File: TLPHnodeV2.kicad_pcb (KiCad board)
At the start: 4 copper layers, 28 x 20.5 mm, 30 parts, among them P1 Bat, P2 CONN_01X07, SW1 Reset, U1 NCP703, U2 LD39130S, U3 LPS25HB, U4 Si7006-A20, U5 ESP-12E, U6 ISL29035

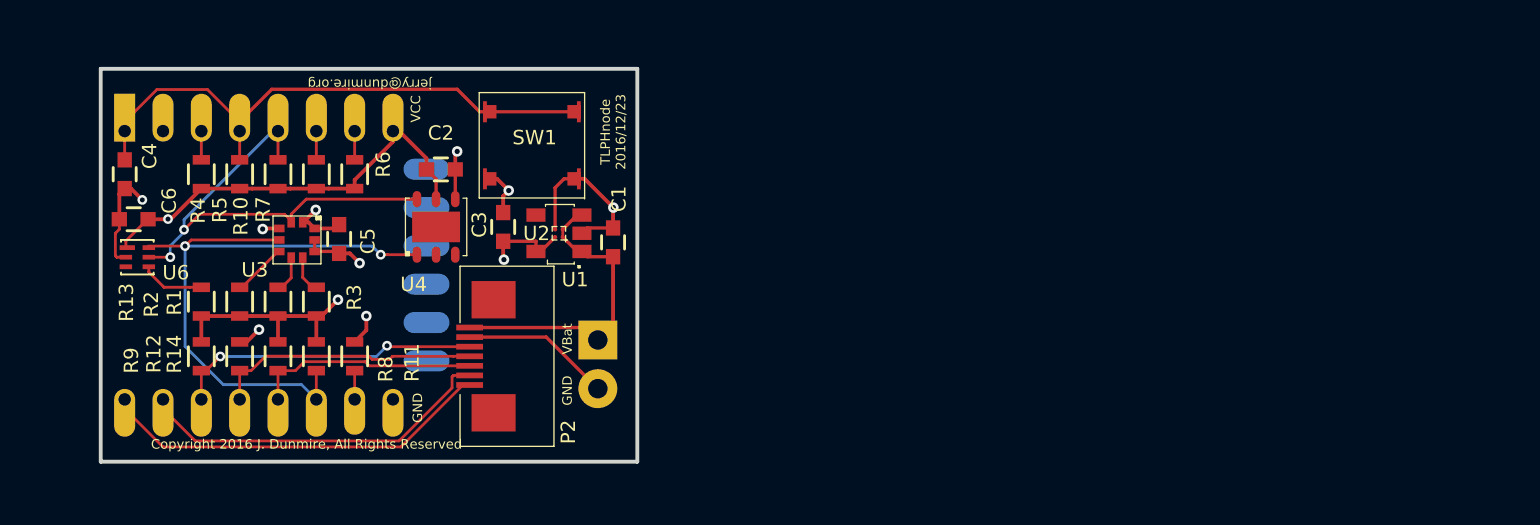
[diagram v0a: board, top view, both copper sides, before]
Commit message: Get ready for new routing
    - remove old parts and all traces
    - import new netlist

On branch master
modified:   TLPHnodeV2.kicad_pcb
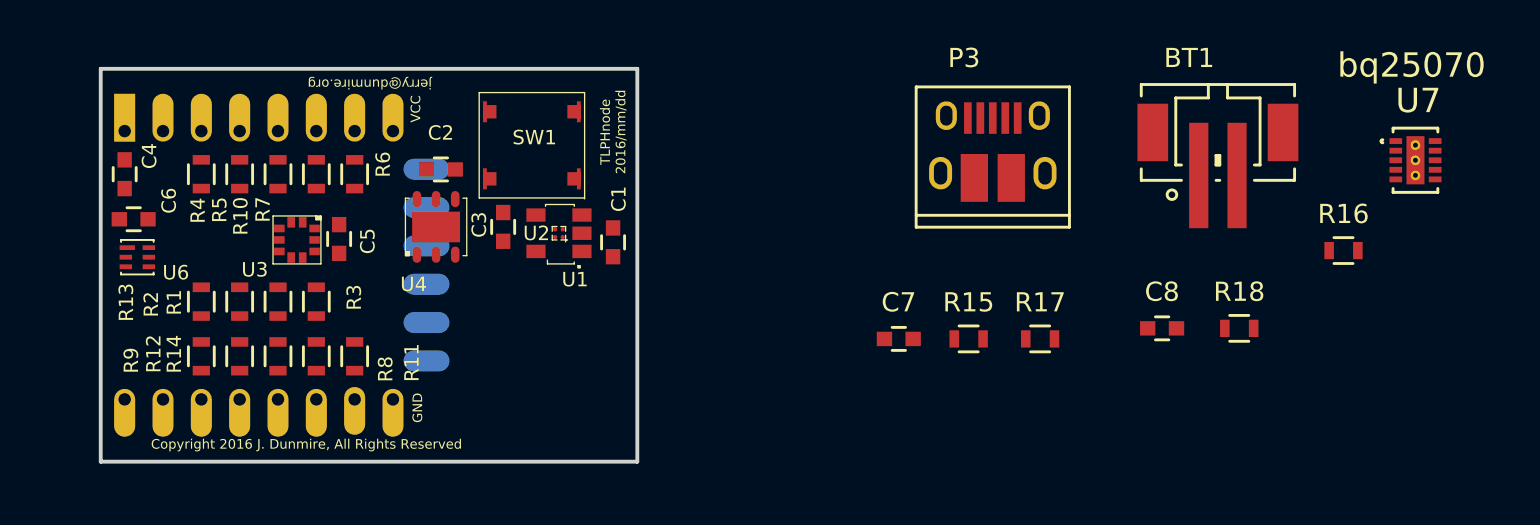
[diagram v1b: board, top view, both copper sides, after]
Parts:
- removed P1: Bat, Pin_Headers:Pin_Header_Straight_1x02
- removed P2: CONN_01X07, rockingdlabs:FPC_conn-7_8x4.9mm_Pitch0.5mm
- removed Ref**: RockingDLogo_9x7, rockingDLogos:RockingDLogo_9x7
- added BT1: LiFeP04, Connectors_JST:JST_PH_B2B-PH-SM4-TB_02x2.00mm_Straight, F.Cu at (188.8, 84.9)
- added C7: 1 uF, Capacitors_SMD:C_0603, F.Cu at (172.1, 94.6)
- added C8: 2 uF, Capacitors_SMD:C_0603, F.Cu at (185.9, 94.0)
- added P3: USB (power only), Connect:USB_Micro-B_10103594-0001LF, F.Cu at (177.1, 84.6)
- added R15: 10k, Resistors_SMD:R_0603, F.Cu at (175.8, 94.6)
- added R16: 1k, Resistors_SMD:R_0603, F.Cu at (195.3, 90.0)
- added R17: 487k, Resistors_SMD:R_0603, F.Cu at (179.5, 94.6)
- added R18: 100k, Resistors_SMD:R_0603, F.Cu at (189.9, 94.0)
- added U7: bq25070, rockingdlabs:bq25070_DQC_10-DQC10_P84X2P4, F.Cu at (199.1, 85.3)
- R12: value 10k -> 4.7k
- R14: value 4.7k -> 10k
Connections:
- net /CHRG renamed /node/CHRG
- net /I2C_SCL renamed /node/I2C_SCL
- net /I2C_SDA renamed /node/I2C_SDA
- net /VBat renamed +BATT
- R12 pad 1: /CTRL -> VCC
- R12 pad 2: GND -> Net-(R12-Pad2)
- R13 pad 2: Net-(R13-Pad2) -> /node/PGM
- R14 pad 1: VCC -> /node/CTRL
- R14 pad 2: /PGM -> GND
- U1 pad 4: Net-(U1-Pad4) -> (no net)
- U5 pad 12: /PGM -> /node/PGM
- U5 pad 13: /CTRL -> /node/CTRL
- U5 pad 15: /RXD -> /node/RXD
- U5 pad 16: /TXD -> /node/TXD
- U5 pad 17: Net-(U5-Pad17) -> (no net)
- U5 pad 18: Net-(U5-Pad18) -> (no net)
- U5 pad 19: Net-(U5-Pad19) -> (no net)
- U5 pad 2: Net-(U5-Pad2) -> (no net)
- U5 pad 20: Net-(U5-Pad20) -> (no net)
- U5 pad 21: Net-(U5-Pad21) -> (no net)
- U5 pad 22: Net-(U5-Pad22) -> (no net)
- U6 pad 3: Net-(U6-Pad3) -> (no net)
- U6 pad 4: Net-(R13-Pad2) -> Net-(R12-Pad2)
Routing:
- net VCC: track 41.0 -> 0.00 mm, vias 4 -> 0
- net GND: track 34.1 -> 0.00 mm, vias 8 -> 0
- net /node/I2C_SDA: track 34.0 -> 0.00 mm, vias 2 -> 0
- net Net-(C4-Pad1): track 30.5 -> 0.00 mm
- net /node/I2C_SCL: track 25.1 -> 0.00 mm, vias 2 -> 0
- net /TXD: track 20.6 -> 0.00 mm
- net /RXD: track 18.9 -> 0.00 mm
- net +BATT: track 16.4 -> 0.00 mm
- net /node/CHRG: track 16.1 -> 0.00 mm, vias 2 -> 0
- net /CTRL: track 13.9 -> 0.00 mm
- net /PGM: track 11.8 -> 0.00 mm
- net Net-(R13-Pad2): track 3.34 -> 0.00 mm
- net Net-(R2-Pad2): track 2.84 -> 0.00 mm
- net Net-(R3-Pad2): track 1.96 -> 0.00 mm
- net Net-(R1-Pad2): track 1.95 -> 0.00 mm
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- removed copper zone on In1.Cu.GND, net GND
- removed copper zone on In2.Cu.VCC, net VCC
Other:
- board text added: "TLPHnode 2016/mm/dd"
- board text removed: "TLPHnode 2016/12/23"
- board text removed: "VBat"

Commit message: CP- initial placement
On branch master
modified:   TLPHnodeV2.kicad_pcb
modified:   TLPHnodeV2.pro
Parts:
- removed C1: 1 uF, Capacitors_SMD:C_0603
- removed R14: 10k, Resistors_SMD:R_0603
- BT1, P3: moved to B.Cu
- moved U7 49.8 mm to (150.5, 96.0), turned to 180 degrees
- moved R16 41.9 mm to (153.8, 95.2)
- moved R15 37.1 mm to (138.8, 95.5), turned to 90 degrees
- moved R18 36.0 mm to (154.0, 91.8)
- moved C8 35.4 mm to (150.5, 93.5)
- moved BT1 35.1 mm to (153.8, 86.2), turned to 90 degrees
- moved P3 24.8 mm to (155.0, 96.0), turned to 270 degrees
- moved R17 22.8 mm to (156.9, 91.8), turned to 180 degrees
- moved C7 18.6 mm to (153.8, 97.0)
- moved R12 5.40 mm to (132.5, 94.2)
- moved R13 5.33 mm to (140.2, 95.5), turned to 270 degrees
- moved U1 4.02 mm to (150.8, 90.9), turned to 180 degrees
- moved U2 3.97 mm to (150.8, 90.8), turned to 90 degrees
- moved U4 3.75 mm to (145.8, 91.8)
- moved C2 3.55 mm to (146.0, 88.5)
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
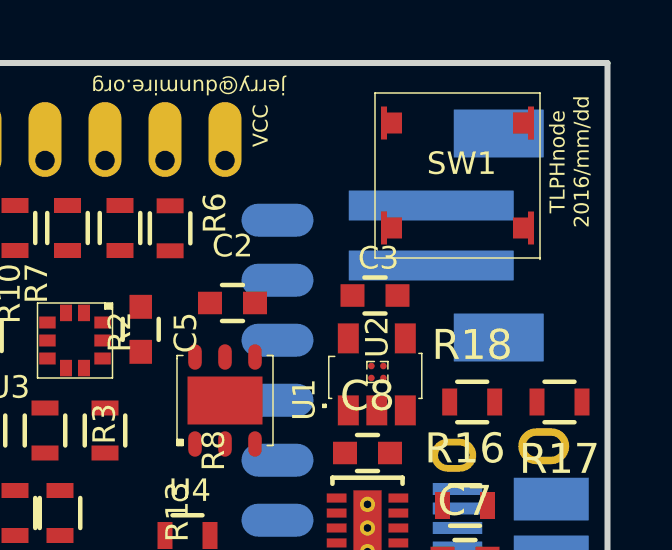
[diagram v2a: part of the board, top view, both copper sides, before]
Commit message: CP - refined placement
    - Rotated battery connector
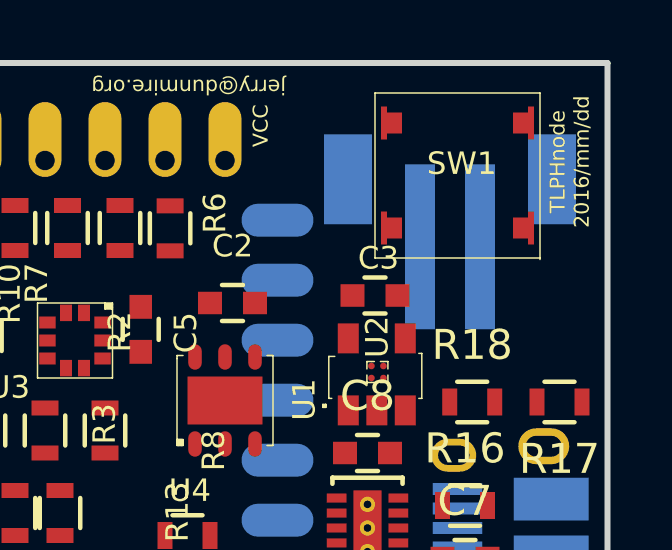
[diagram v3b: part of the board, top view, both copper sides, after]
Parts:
- moved BT1 0.90 mm to (153.2, 85.5), turned to 180 degrees
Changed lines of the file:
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@@
   )
   (module Connectors_JST:JST_PH_B2B-PH-SM4-TB_02x2.00mm_Straight (layer B.Cu)
-    (at 153.75 86.25 90)
+    (at 153.25 85.5 180)
     (descr http://www.jst-mfg.com/product/pdf/eng/ePH.pdf)
     (tags "connector jst ph")
     (attr smd)
-    (fp_text reference BT1 (at -1.5 5 90) (layer B.SilkS)
+    (fp_text reference BT1 (at -1.5 5 180) (layer B.SilkS)
       (effects (font (size 1 1) (thickness 0.15)) (justify mirror))
     )
-    (fp_text value LiFeP04 (at 0 -5.25 90) (layer B.Fab)
+    (fp_text value LiFeP04 (at 0 -5.25 180) (layer B.Fab)
       (effects (font (size 1 1) (thickness 0.15)) (justify mirror))
     )
@@
     (fp_line (start -4 3.025) (end -4 3.625) (layer B.SilkS) (width 0.15))
     (fp_circle (center -2.4 -2.125) (end -2.15 -2.125) (layer B.SilkS) (width 0.15))
-    (pad "" smd rect (at 3.4 1.125 90) (size 1.6 3) (layers B.Cu B.Paste B.Mask))
-    (pad "" smd rect (at -3.4 1.125 90) (size 1.6 3) (layers B.Cu B.Paste B.Mask))
-    (pad 2 smd rect (at 1 -1.125 90) (size 1 5.5) (layers B.Cu B.Paste B.Mask)
+    (pad "" smd rect (at 3.4 1.125 180) (size 1.6 3) (layers B.Cu B.Paste B.Mask))
+    (pad "" smd rect (at -3.4 1.125 180) (size 1.6 3) (layers B.Cu B.Paste B.Mask))
+    (pad 2 smd rect (at 1 -1.125 180) (size 1 5.5) (layers B.Cu B.Paste B.Mask)
       (net 1 GND))
-    (pad 1 smd rect (at -1 -1.125 90) (size 1 5.5) (layers B.Cu B.Paste B.Mask)
+    (pad 1 smd rect (at -1 -1.125 180) (size 1 5.5) (layers B.Cu B.Paste B.Mask)
       (net 11 +BATT))
+    (model ${ROCKINGDLIB}/rockingdlabs.3dshapes/B2B-PH-SM4-TB.STEP
+      (at (xyz -0.1574803149606299 0.09842519685039371 0))
+      (scale (xyz 1 1 1))
+      (rotate (xyz -90 0 0))
+    )
   )
   (module Capacitors_SMD:C_0603 (layer F.Cu)
@@
     (pad 1 smd rect (at -1.3 1.5 180) (size 1.65 0.4) (layers B.Cu B.Paste B.Mask)
       (net 12 /power/VDD))
+    (model ${ROCKINGDLIB}/rockingdlabs.3dshapes/10103594.stp
+      (at (xyz 0 0 0.08858267716535434))
+      (scale (xyz 1 1 1))
+      (rotate (xyz 90 0 180))
+    )
   )
   (module Resistors_SMD:R_0603 (layer F.Cu)

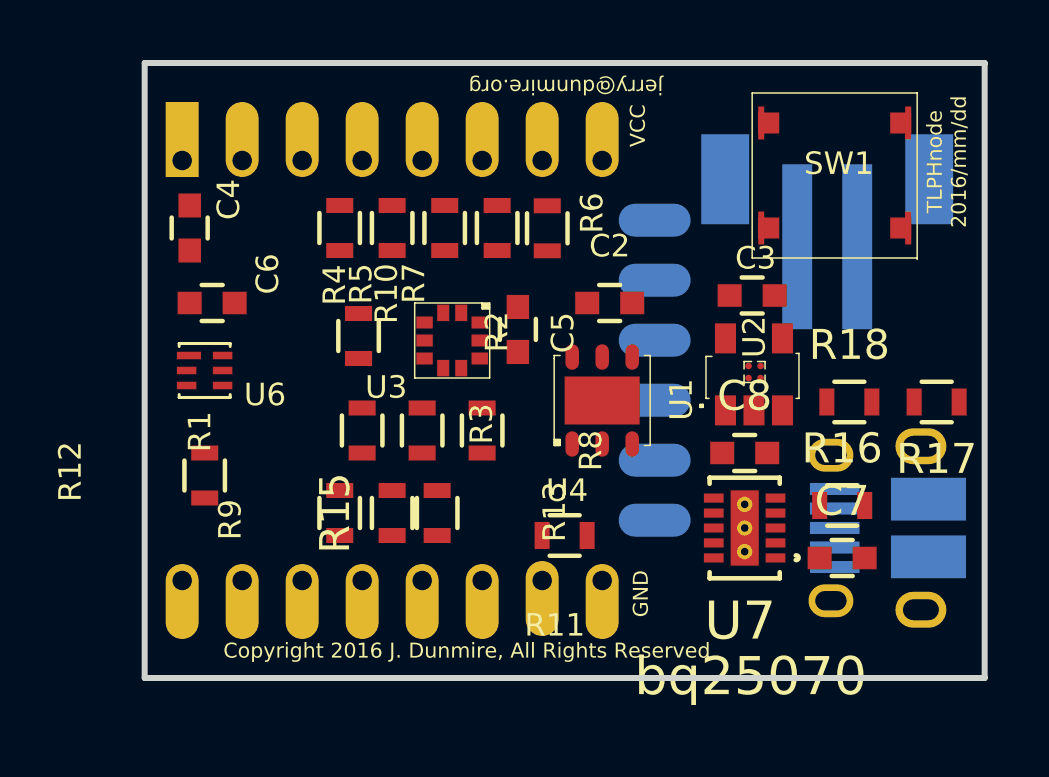
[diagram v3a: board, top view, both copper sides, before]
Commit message: CP - routing started
    - Need two swap CTRL and CHRG to make routing cleaner
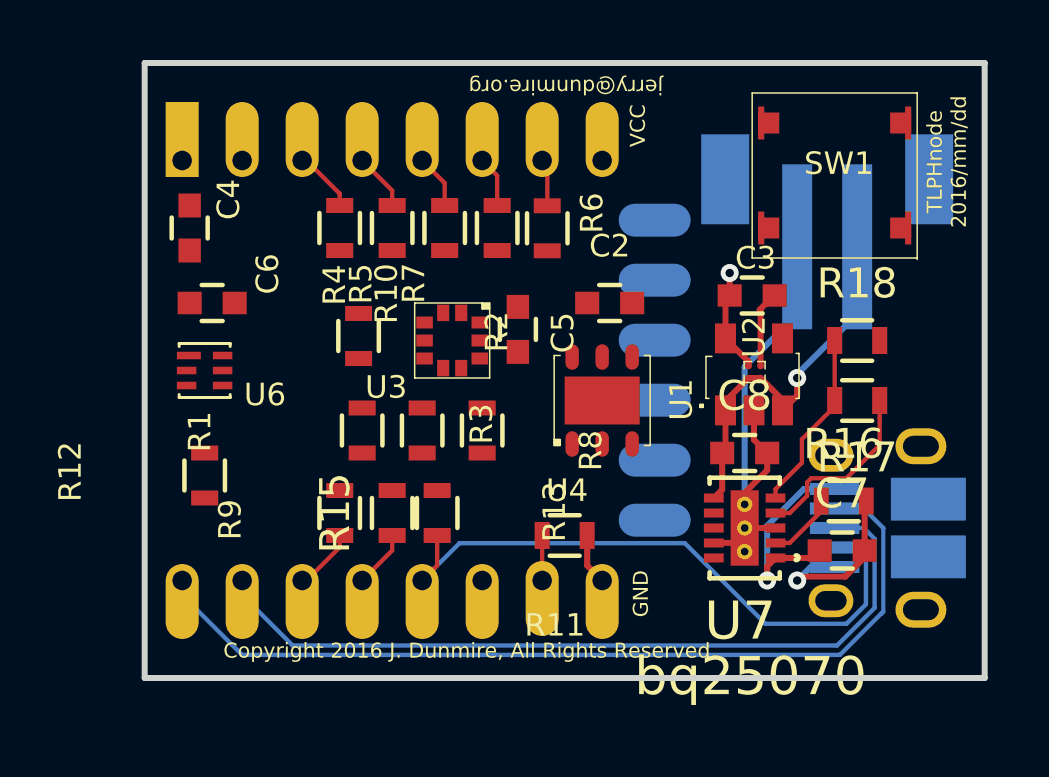
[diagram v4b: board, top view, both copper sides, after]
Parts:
- moved R17 2.65 mm to (154.2, 91.8)
- moved R18 2.07 mm to (154.2, 89.8)
- moved C7 0.25 mm to (153.8, 96.8)
- moved R16 0.16 mm to (153.8, 95.1)
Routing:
- net /node/TXD: track 0.00 -> 30.0 mm
- net /node/RXD: track 0.00 -> 26.6 mm
- net GND: track 0.00 -> 25.2 mm, vias 0 -> 1
- net /node/PGM: track 0.00 -> 21.3 mm
- net +BATT: track 0.00 -> 12.8 mm, vias 0 -> 1
- net /power/VDD: track 0.00 -> 6.92 mm, vias 0 -> 1
- net +3V3: track 0.00 -> 6.16 mm
- net Net-(R17-Pad2): track 0.00 -> 6.07 mm
- net VCC: track 0.00 -> 3.48 mm, vias 0 -> 1
- net Net-(R16-Pad1): track 0.00 -> 2.31 mm
- net Net-(R4-Pad2): track 0.00 -> 2.10 mm
- net /node/CHRG: track 0.00 -> 2.10 mm
- net Net-(C4-Pad1): track 0.00 -> 1.91 mm
- net /node/CTRL: track 0.00 -> 1.91 mm
- net /node/I2C_SCL: track 0.00 -> 1.81 mm
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
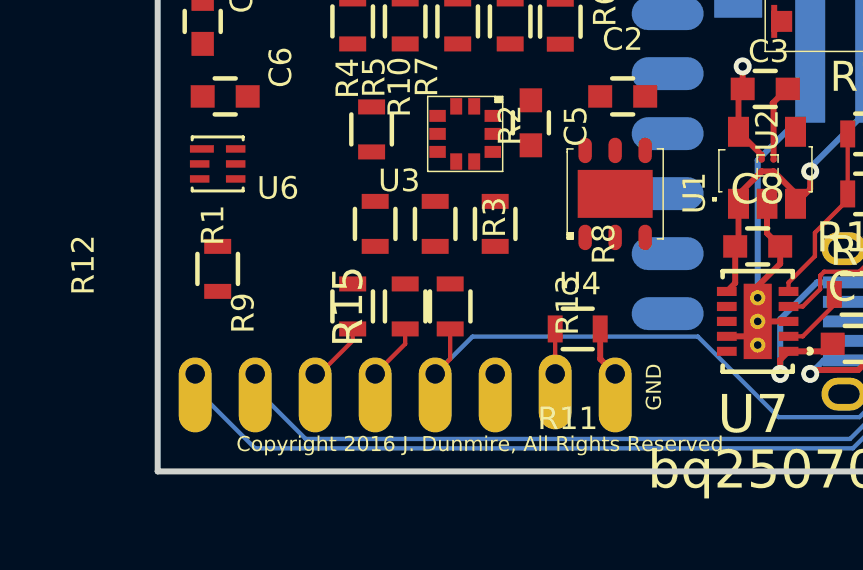
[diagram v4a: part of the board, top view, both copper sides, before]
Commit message: Swap ESP-8266 signals for charger control
    - Swap CHRG and CTRL to make layout cleaner

On branch master
modified:   TLPHnodeV2.kicad_pcb
modified:   TLPHnodeV2.net
modified:   node.sch
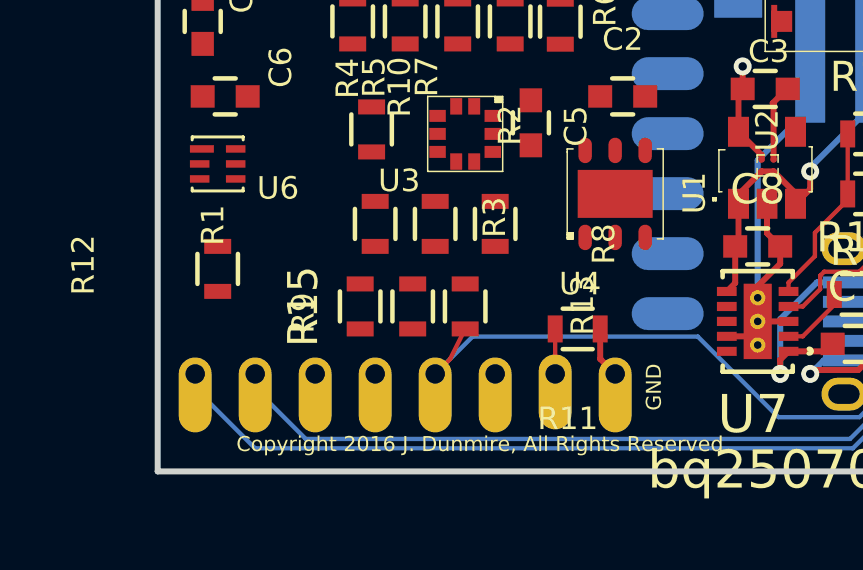
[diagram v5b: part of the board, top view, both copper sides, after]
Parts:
- moved R9 2.00 mm to (139.0, 95.5)
- moved R15 1.50 mm to (137.2, 95.5)
- moved R13 0.50 mm to (140.8, 95.5)
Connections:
- U5 pad 13: /node/CTRL -> /node/CHRG
- U5 pad 14: /node/CHRG -> /node/CTRL
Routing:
- net /node/CHRG: track 2.10 -> 0.00 mm
- net /node/CTRL: track 1.91 -> 0.14 mm
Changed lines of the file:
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@@
   (general
     (links 96)
-    (no_connects 54)
+    (no_connects 56)
     (area 130.399999 80.399999 158.600001 101.100001)
     (thickness 1.6)
     (drawings 9)
-    (tracks 116)
+    (tracks 112)
     (zones 0)
     (modules 34)
@@
       (net 13 /node/PGM))
     (pad 13 thru_hole oval (at 14 -6 270) (size 2.5 1.1) (drill 0.65 (offset 0.7 0)) (layers *.Cu *.Mask B.SilkS)
+      (net 17 /node/CHRG))
+    (pad 14 thru_hole oval (at 14 -4 270) (size 2.5 1.1) (drill 0.65 (offset 0.7 0)) (layers *.Cu *.Mask B.SilkS)
       (net 20 /node/CTRL))
-    (pad 14 thru_hole oval (at 14 -4 270) (size 2.5 1.1) (drill 0.65 (offset 0.7 0)) (layers *.Cu *.Mask B.SilkS)
-      (net 17 /node/CHRG))
     (pad 15 thru_hole oval (at 14 -2 270) (size 2.5 1.1) (drill 0.65 (offset 0.7 0)) (layers *.Cu *.Mask B.SilkS)
       (net 14 /node/RXD))
@@
   )
   (module Resistors_SMD:R_0603 (layer F.Cu)
-    (at 137 95.5 270)
+    (at 139 95.5 270)
     (descr "Resistor SMD 0603, reflow soldering, Vishay (see dcrcw.pdf)")
     (tags "resistor 0603")
@@
   )
   (module Resistors_SMD:R_0603 (layer F.Cu)
-    (at 140.25 95.5 270)
+    (at 140.75 95.5 270)
     (descr "Resistor SMD 0603, reflow soldering, Vishay (see dcrcw.pdf)")
     (tags "resistor 0603")
@@
   )
   (module Resistors_SMD:R_0603 (layer F.Cu)
-    (at 138.75 95.5 90)
+    (at 137.25 95.5 90)
     (descr "Resistor SMD 0603, reflow soldering, Vishay (see dcrcw.pdf)")
     (tags "resistor 0603")
@@
   (segment (start 140.99282 96.50718) (end 148.50718 96.50718) (width 0.14478) (layer B.Cu) (net 13))
   (segment (start 139.75 97.75) (end 140.25 97.25) (width 0.14478) (layer F.Cu) (net 13))
-  (segment (start 140.25 97.25) (end 140.25 96.25) (width 0.14478) (layer F.Cu) (net 13))
+  (segment (start 140.25 97.25) (end 140.75 96.25) (width 0.14478) (layer F.Cu) (net 13) (status 20))
   (segment (start 154.831742 96.361062) (end 154.46978 95.9991) (width 0.14478) (layer B.Cu) (net 14))
   (segment (start 154.46978 95.9991) (end 153.5 95.9991) (width 0.14478) (layer B.Cu) (net 14))
@@
   (segment (start 131.75 97.75) (end 131.75 98.234956) (width 0.14478) (layer B.Cu) (net 15))
   (segment (start 131.75 98.234956) (end 133.745044 100.23) (width 0.14478) (layer B.Cu) (net 15))
-  (segment (start 135.75 97.75) (end 135.89478 97.75) (width 0.14478) (layer F.Cu) (net 17))
-  (segment (start 137 96.64478) (end 137 96.25) (width 0.14478) (layer F.Cu) (net 17))
-  (segment (start 135.89478 97.75) (end 137 96.64478) (width 0.14478) (layer F.Cu) (net 17))
   (segment (start 139.75 83.75) (end 140.5 84.5) (width 0.14478) (layer F.Cu) (net 18))
   (segment (start 140.5 84.5) (end 140.5 85.25) (width 0.14478) (layer F.Cu) (net 18))
-  (segment (start 137.75 97.75) (end 138.75 96.75) (width 0.14478) (layer F.Cu) (net 20))
-  (segment (start 138.75 96.75) (end 138.75 96.25) (width 0.14478) (layer F.Cu) (net 20))
+  (segment (start 135.75 97.75) (end 135.89478 97.75) (width 0.14478) (layer F.Cu) (net 20))
   (segment (start 151.5287 96.49784) (end 152.00368 96.49784) (width 0.14478) (layer F.Cu) (net 21))
   (segment (start 152.00368 96.49784) (end 153.05 95.45152) (width 0.14478) (layer F.Cu) (net 21))
